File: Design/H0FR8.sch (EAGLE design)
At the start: 44 parts, among them Q1 MMBT3904LT1, U1 STM32G0B1CEU6QFN_B1CEU6_STM-L, U2 T2035H-6GD2PAK_T2550_STM-M, U3 VOT8121AM-VT, U4 TLP184_GR-TPL,SE, U5 V275LA4P, X1 XTALL_CSTCE8M00G52

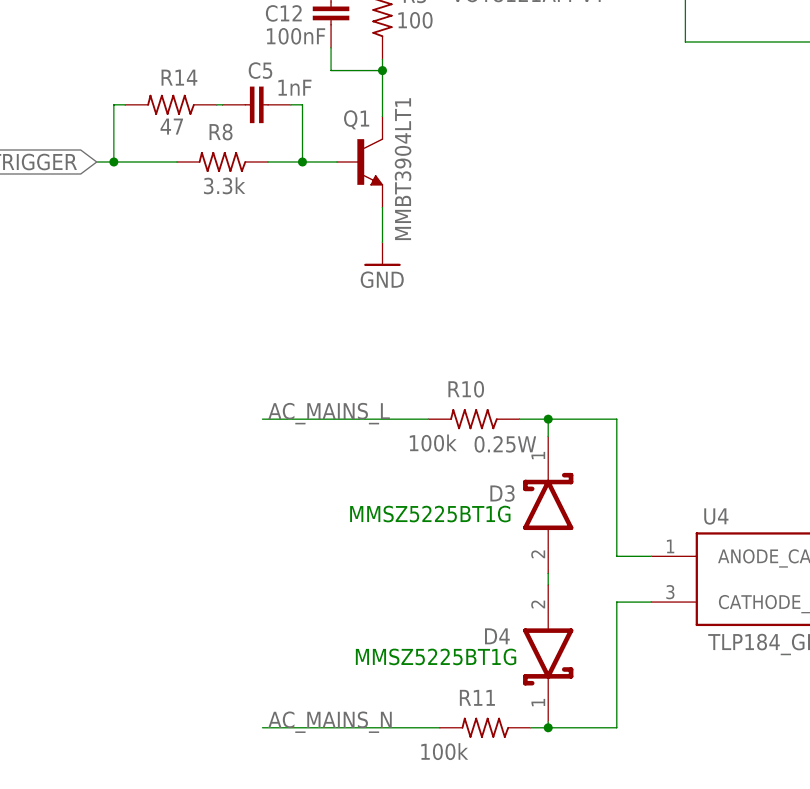
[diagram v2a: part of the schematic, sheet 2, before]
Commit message: - Changed components description in BOM - Fixed issues in Layout - Fixed issues in Schematic - Generated new documentation
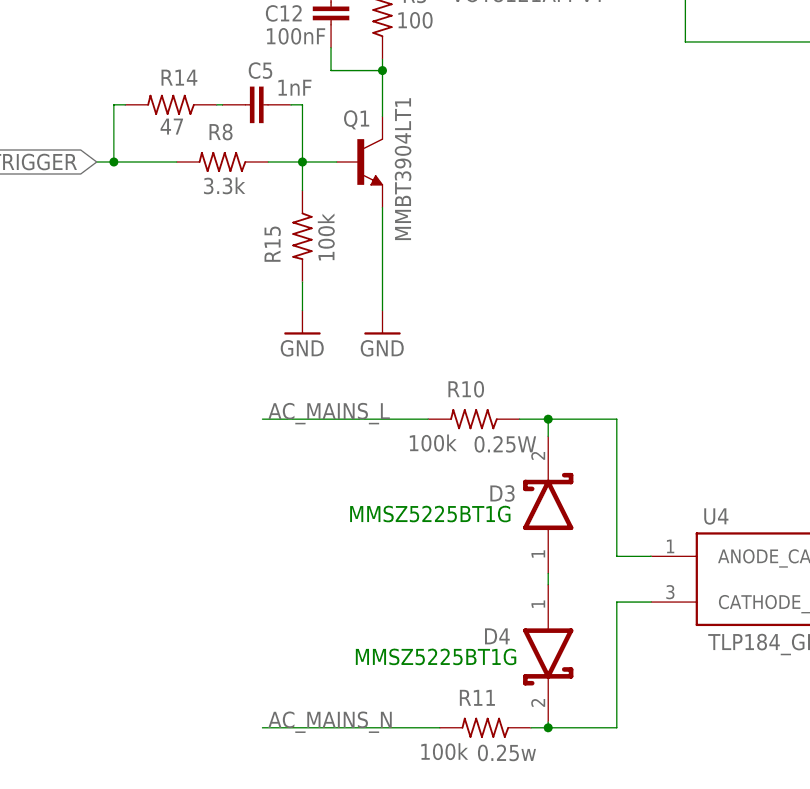
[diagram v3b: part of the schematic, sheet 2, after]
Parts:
- added R15: 100k, HEXABITZ_RCLS:R-0603
- R11: POWER (none) -> 0.25w
- SWD: device pinhead:PINHD-1X3 -> HEXABITZ_CONNECTION_PARTS:PINHD-1X3
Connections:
- net GND: now also R15.2
- net N$13: now also R15.1
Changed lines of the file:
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@@
 <part name="FB1" library="HEXABITZ_RCLS" library_urn="urn:adsk.eagle:library:20064561" deviceset="FB-0603" device="" package3d_urn="urn:adsk.eagle:package:19666458/5"/>
 <part name="SUPPLY10" library="supply2" library_urn="urn:adsk.eagle:library:372" deviceset="VDD" device=""/>
-<part name="SWD" library="pinhead" library_urn="urn:adsk.eagle:library:325" deviceset="PINHD-1X3" device="" package3d_urn="urn:adsk.eagle:package:22458/2"/>
+<part name="SWD" library="HEXABITZ_CONNECTION_PARTS" library_urn="urn:adsk.eagle:library:20064553" deviceset="PINHD-1X3" device="" package3d_urn="urn:adsk.eagle:package:42172678/1"/>
 <part name="U1" library="HEXABITZ_ICs" library_urn="urn:adsk.eagle:library:20064554" deviceset="STM32G0B1CEU6" device="QFN_B1CEU6_STM-L" package3d_urn="urn:adsk.eagle:package:33547754/8"/>
 <part name="TRIMBLE-LOGO1" library="HEXABITZ_USER_INTERFACE_PARTS" library_urn="urn:adsk.eagle:library:20064563" deviceset="HEXA-LOGO-SCH" device=""/>
@@
 <part name="R11" library="HEXABITZ_RCLS" library_urn="urn:adsk.eagle:library:20064561" deviceset="R-0805" device="" package3d_urn="urn:adsk.eagle:package:19666457/4" value="100k">
 <attribute name="MPN" value="ERJ-P06J104V"/>
+<attribute name="POWER" value="0.25w"/>
 </part>
 <part name="R14" library="HEXABITZ_RCLS" library_urn="urn:adsk.eagle:library:20064561" deviceset="R-0603" device="" package3d_urn="urn:adsk.eagle:package:1435818/6" value="47">
@@
 <part name="LOAD" library="HEXABITZ_CONNECTION_PARTS" library_urn="urn:adsk.eagle:library:20064553" deviceset="1546111-2" device="" package3d_urn="urn:adsk.eagle:package:19666461/4"/>
 <part name="AC_MAINS" library="HEXABITZ_CONNECTION_PARTS" library_urn="urn:adsk.eagle:library:20064553" deviceset="1546111-2" device="" package3d_urn="urn:adsk.eagle:package:19666461/4"/>
+<part name="R15" library="HEXABITZ_RCLS" library_urn="urn:adsk.eagle:library:20064561" deviceset="R-0603" device="" package3d_urn="urn:adsk.eagle:package:1435818/6" value="100k">
+<attribute name="MFN" value="Yageo"/>
+<attribute name="MPN" value="RC0603JR-070RL"/>
+<attribute name="OCTOPART_URL" value="https://octopart.com/crcw06032k40jnea-vishay-40298967"/>
+<attribute name="RESISTANCE" value="2400.0 Ω"/>
+<attribute name="TOLERANCE" value="±5%"/>
+</part>
+<part name="GND3" library="supply1" library_urn="urn:adsk.eagle:library:371" deviceset="GND" device=""/>
 </parts>
 <sheets>
@@
 </segment>
 </net>
-<net name="VSSA" class="1">
+<net name="VSSA" class="0">
 <segment>
 <pinref part="SUPPLY3" gate="G$1" pin="VSSA"/>
@@
 <attribute name="VALUE" x="62.23" y="112.522" size="1.778" layer="96" rot="R180"/>
 </instance>
-<instance part="GND4" gate="1" x="77.47" y="102.87" smashed="yes">
-<attribute name="VALUE" x="74.93" y="100.33" size="1.778" layer="96"/>
+<instance part="GND4" gate="1" x="77.47" y="95.25" smashed="yes">
+<attribute name="VALUE" x="74.93" y="92.71" size="1.778" layer="96"/>
 </instance>
 <instance part="C12" gate="G$1" x="71.755" y="129.54" smashed="yes">
@@
 <attribute name="NAME" x="90.17" y="55.6514" size="1.778" layer="95" rot="R180"/>
 <attribute name="VALUE" x="86.995" y="49.657" size="1.778" layer="96" rot="R180"/>
+<attribute name="POWER" x="94.615" y="49.53" size="1.778" layer="96" rot="R180"/>
 </instance>
 <instance part="R14" gate="G$1" x="53.975" y="120.65" smashed="yes" rot="R180">
@@
 <attribute name="VALUE" x="240.03" y="159.258" size="1.27" layer="96" rot="R180"/>
 </instance>
+<instance part="R15" gate="G$1" x="68.58" y="106.045" smashed="yes" rot="R270">
+<attribute name="NAME" x="64.3636" y="107.315" size="1.778" layer="95" rot="R270"/>
+<attribute name="VALUE" x="70.358" y="108.585" size="1.778" layer="96" rot="R270"/>
+</instance>
+<instance part="GND3" gate="1" x="68.58" y="95.25" smashed="yes">
+<attribute name="VALUE" x="66.04" y="92.71" size="1.778" layer="96"/>
+</instance>
 </instances>
 <busses>
@@
 <wire x1="68.58" y1="120.65" x2="68.58" y2="114.3" width="0.1524" layer="91"/>
 <junction x="68.58" y="114.3"/>
+<pinref part="R15" gate="G$1" pin="1"/>
+<wire x1="68.58" y1="111.125" x2="68.58" y2="114.3" width="0.1524" layer="91"/>
 </segment>
 </net>
@@
 <pinref part="Q1" gate="G$1" pin="E"/>
 <pinref part="GND4" gate="1" pin="GND"/>
-<wire x1="77.47" y1="109.22" x2="77.47" y2="105.41" width="0.1524" layer="91"/>
+<wire x1="77.47" y1="109.22" x2="77.47" y2="97.79" width="0.1524" layer="91"/>
 </segment>
 <segment>
@@
 <wire x1="163.195" y1="57.15" x2="163.195" y2="59.69" width="0.1524" layer="91"/>
 </segment>
+<segment>
+<pinref part="GND3" gate="1" pin="GND"/>
+<pinref part="R15" gate="G$1" pin="2"/>
+<wire x1="68.58" y1="97.79" x2="68.58" y2="100.965" width="0.1524" layer="91"/>
+</segment>
 </net>

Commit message: -The final design, all done.
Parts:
- removed D3, D4: STMICROELECTRONICS_BAT46ZFILMSTMICROELECTRONICS_BAT46ZFILM_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, HEXABITZ_RCLS:STMICROELECTRONICS_BAT46ZFILMSTMICROELECTRONICS_BAT46ZFILM_0_3
- removed U2: T2035H-6GD2PAK_T2550_STM-M, HEXABITZ_ICs:T2035H-6GD2PAK_T2550_STM-M
- added Q2: T2035H-6G, HEXABITZ_ICs:T2035H-6G
- added Z1, Z2: MMSZ5225BT1G, HEXABITZ_RCLS:MMSZ5225BT1G
- C2, C3: device HEXABITZ_RCLS:C-0603-POL -> HEXABITZ_RCLS:C-0805-POL
- D1: device Hexabitz:VLMS1300-GS08 -> HEXABITZ_USER_INTERFACE_PARTS:VLMS1300-GS08
- renumbered U5 to VDR1
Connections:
- removed net N$14: D3.ANODE, D4.ANODE
- removed net USART4_RX: U$1.SD1, U1.PA1
- removed net USART4_TX: U$1.SU1, U1.PA0
- new net N$12: Z1.A, Z2.A
- net A2: now also LOAD.1, Q2.MT2; no longer LOAD.2, U2.A2
- net AC_MAINS_L: now also AC_MAINS.1, LOAD.2; no longer AC_MAINS.2, LOAD.1
- net AC_MAINS_N: now also AC_MAINS.2, Q2.MT1; no longer AC_MAINS.1, U2.A1
- net LED_INDICATOR: now also U1.PA11_[PA9]; no longer U1.PB13
- net N$15: now also Z1.K; no longer D3.CATHODE
- net N$16: now also Z2.K; no longer D4.CATHODE
- net TRIAC_G: now also Q2.G; no longer U2.G
- net TRIAC_TRIGGER: now also U1.PA6; no longer U1.PB1
- net USART1_RX: now also U$1.SD3; no longer U$1.SD4
- net USART1_TX: now also U$1.SU3; no longer U$1.SU4
- net USART5_RX: now also U$1.SD4
- net USART5_TX: now also U$1.SU4
- net USART6_RX: now also U$1.SD1, U1.PB9; no longer U$1.SD3, U1.PA5
- net USART6_TX: now also U$1.SU1, U1.PB8; no longer U$1.SU3, U1.PA4
- net VDDA: now also C2.+, C3.+; no longer C2.1, C3.1
- net VSSA: now also C2.-, C3.-; no longer C2.2, C3.2
- net ZC_DETECT: now also U1.PB7; no longer U1.PB0
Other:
- note removed: "MMSZ5225BT1G"
- moved on the sheet: AC_MAINS, C1, C2, C3, C7, C8, D1, D2, FB1, LOAD, R, R1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
